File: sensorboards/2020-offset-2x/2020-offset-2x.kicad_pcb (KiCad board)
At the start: 2 copper layers, 45.5 x 45.2 mm, 8 parts, among them J1 Conn_01x10_Male, U1 CNY70, U2 CNY70, U3 CNY70, U4 CNY70

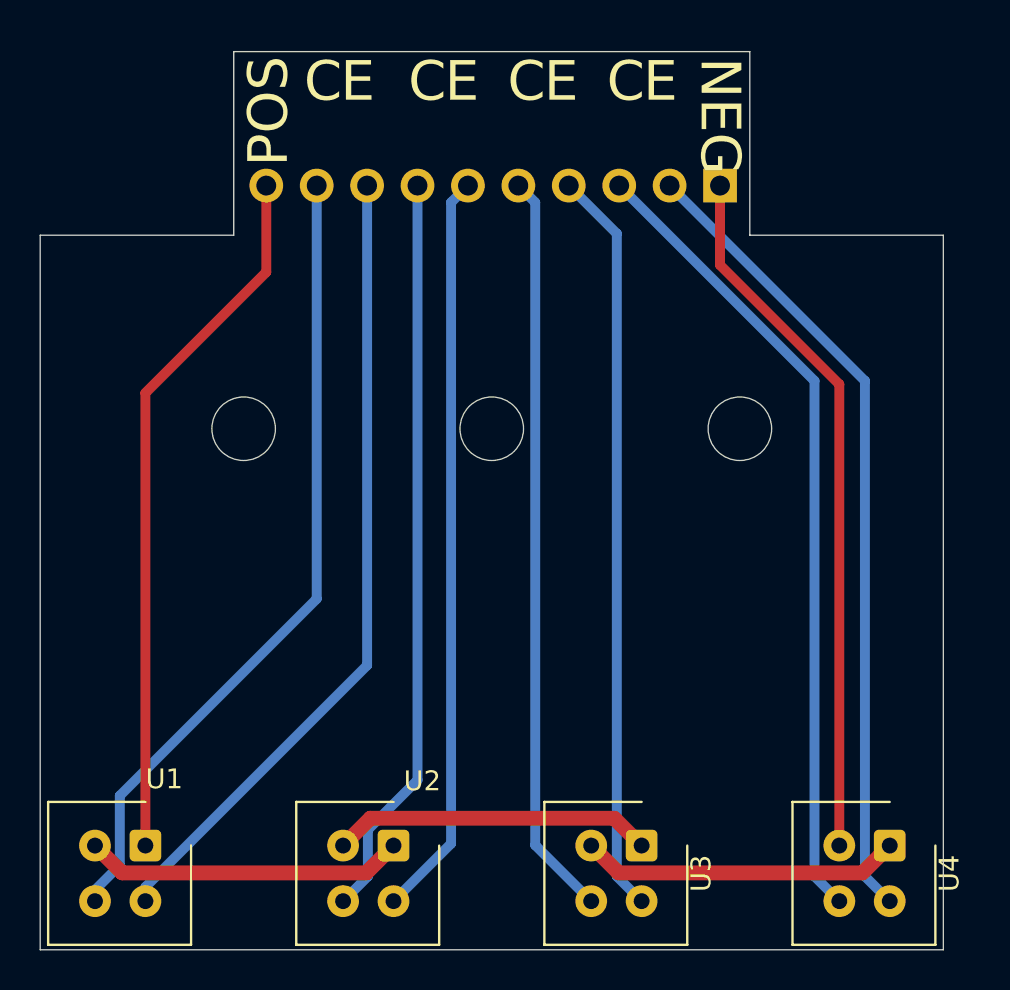
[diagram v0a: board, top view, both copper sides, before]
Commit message: Made issue #44 changes to sensorboards, introduced 3x versions
Also finished bringing them up to Kicad 6.0
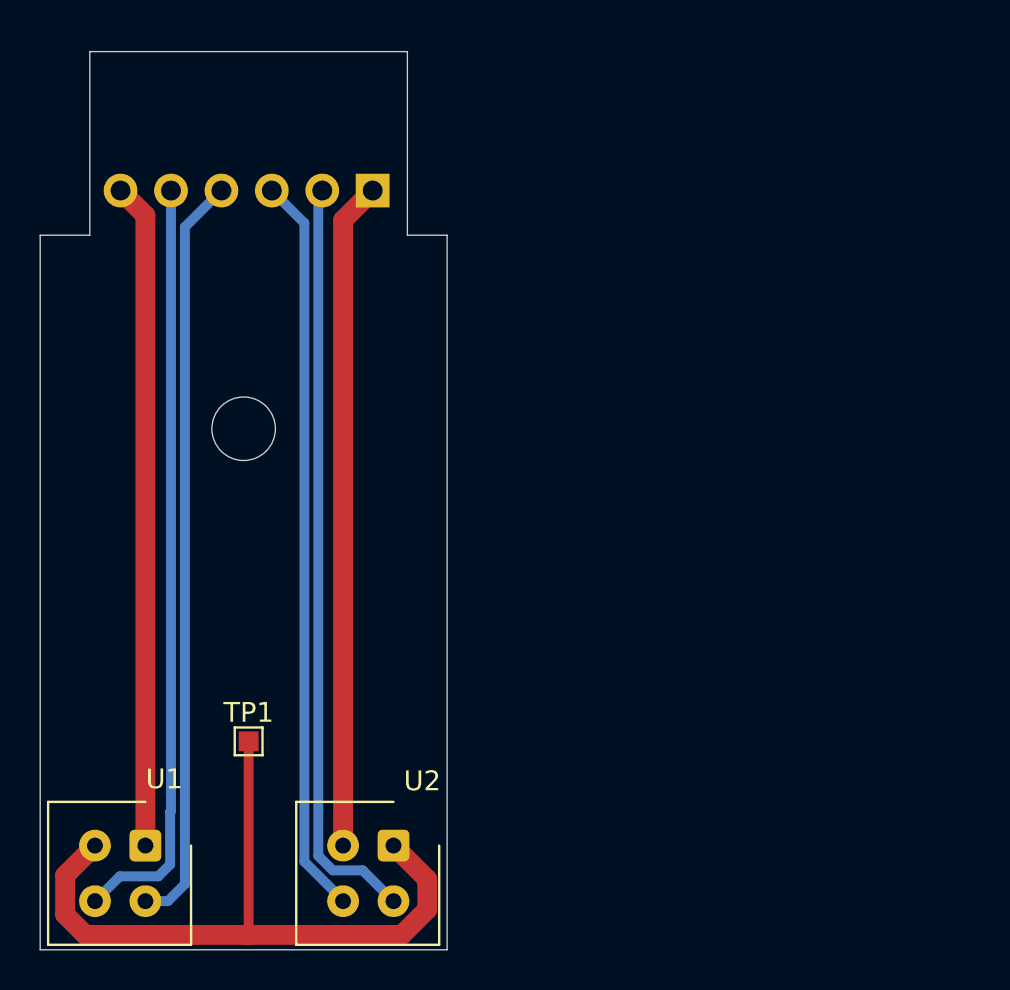
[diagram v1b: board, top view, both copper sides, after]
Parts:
- removed H2, H3: MountingHole, Mounting_Holes:MountingHole_3.2mm_M3
- removed U3, U4: CNY70, OptoDevice:Vishay_CNY70
- added TP1: TestPoint, TestPoint:TestPoint_Pad_1.0x1.0mm, F.Cu at (160.0, 125.8)
- J1: value Conn_01x10_Male -> Conn_01x06_Male; footprint Pin_Headers:Pin_Header_Angled_1x10_Pitch2.54mm -> Pin_Headers:Pin_Header_Angled_1x06_Pitch2.54mm
- moved J1 17.5 mm to (166.2, 98.0)
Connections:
- J1 pad 2: /E4 -> /E2
- J1 pad 3: /C4 -> /C2
- J1 pad 4: /E3 -> /E1
- J1 pad 5: /C3 -> /C1
- J1 pad 6: /E2 -> /POS
- U2 pad 2: Net-(U2-Pad2) -> /NEG
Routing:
- net /E4: track 40.6 -> 0.00 mm
- net /C4: track 40.6 -> 0.00 mm
- net /E3: track 37.6 -> 0.00 mm
- net /C3: track 37.6 -> 0.00 mm
- net Net-(U1-Pad2): track 16.2 -> 37.0 mm
- net Net-(U2-Pad2): track 16.2 -> 0.00 mm
- net Net-(U3-Pad2): track 16.2 -> 0.00 mm
- net /E1: track 40.7 -> 38.0 mm
- net /POS: track 35.8 -> 33.5 mm
- net /C1: track 40.7 -> 38.5 mm
- net /NEG: track 35.7 -> 33.6 mm
- net /E2: track 37.6 -> 38.3 mm
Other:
- board size 45.5 x 45.2 mm -> 20.5 x 45.2 mm
- net class Default removed
